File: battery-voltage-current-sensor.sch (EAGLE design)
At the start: 59 parts, among them IC1 ACS758LCB-050B-PFF-T, IC3 ADS1115IDGST

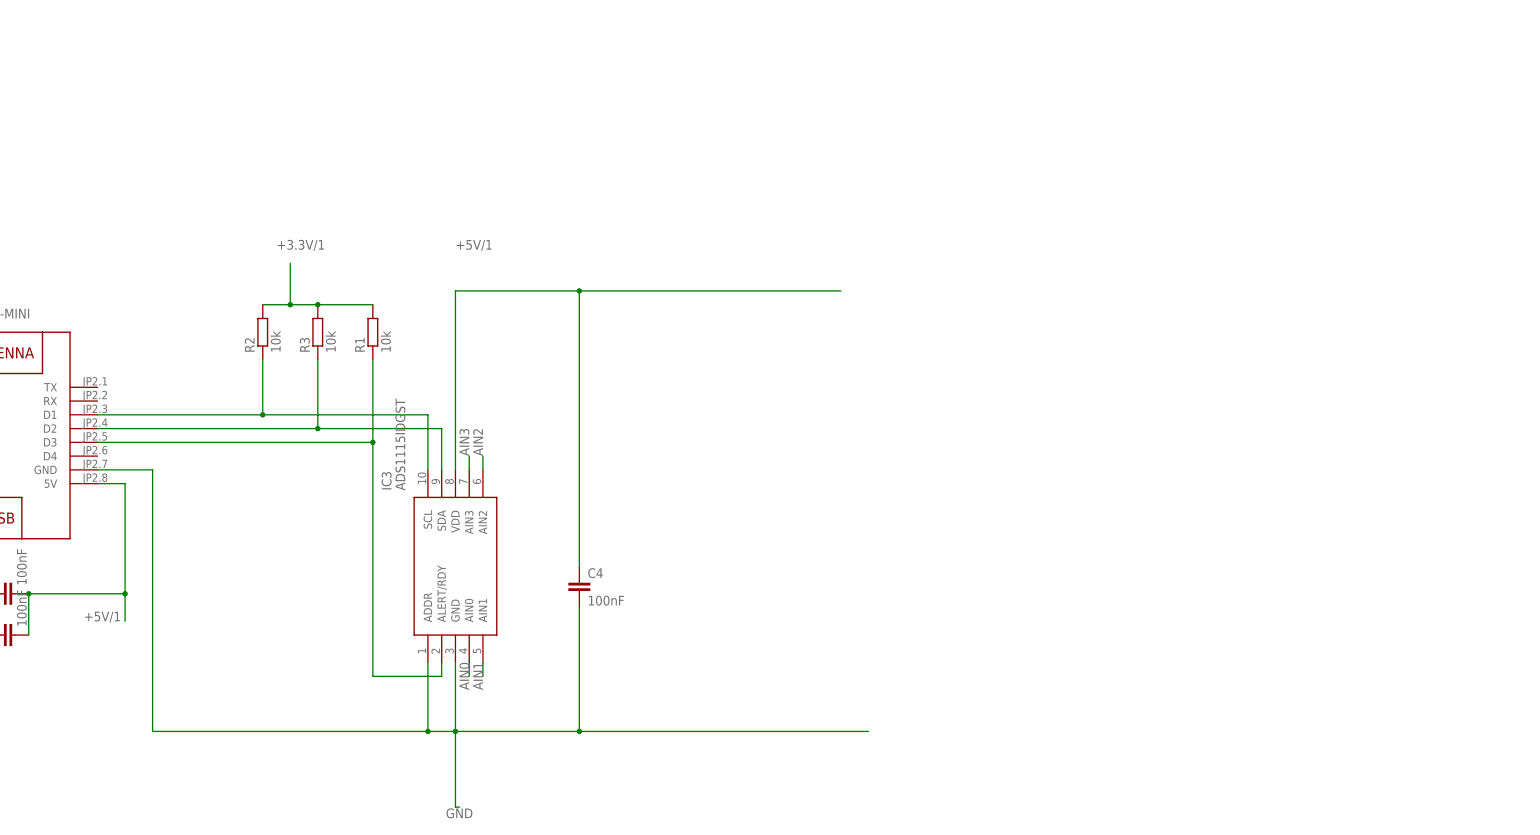
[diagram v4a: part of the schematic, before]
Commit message: level shifter added
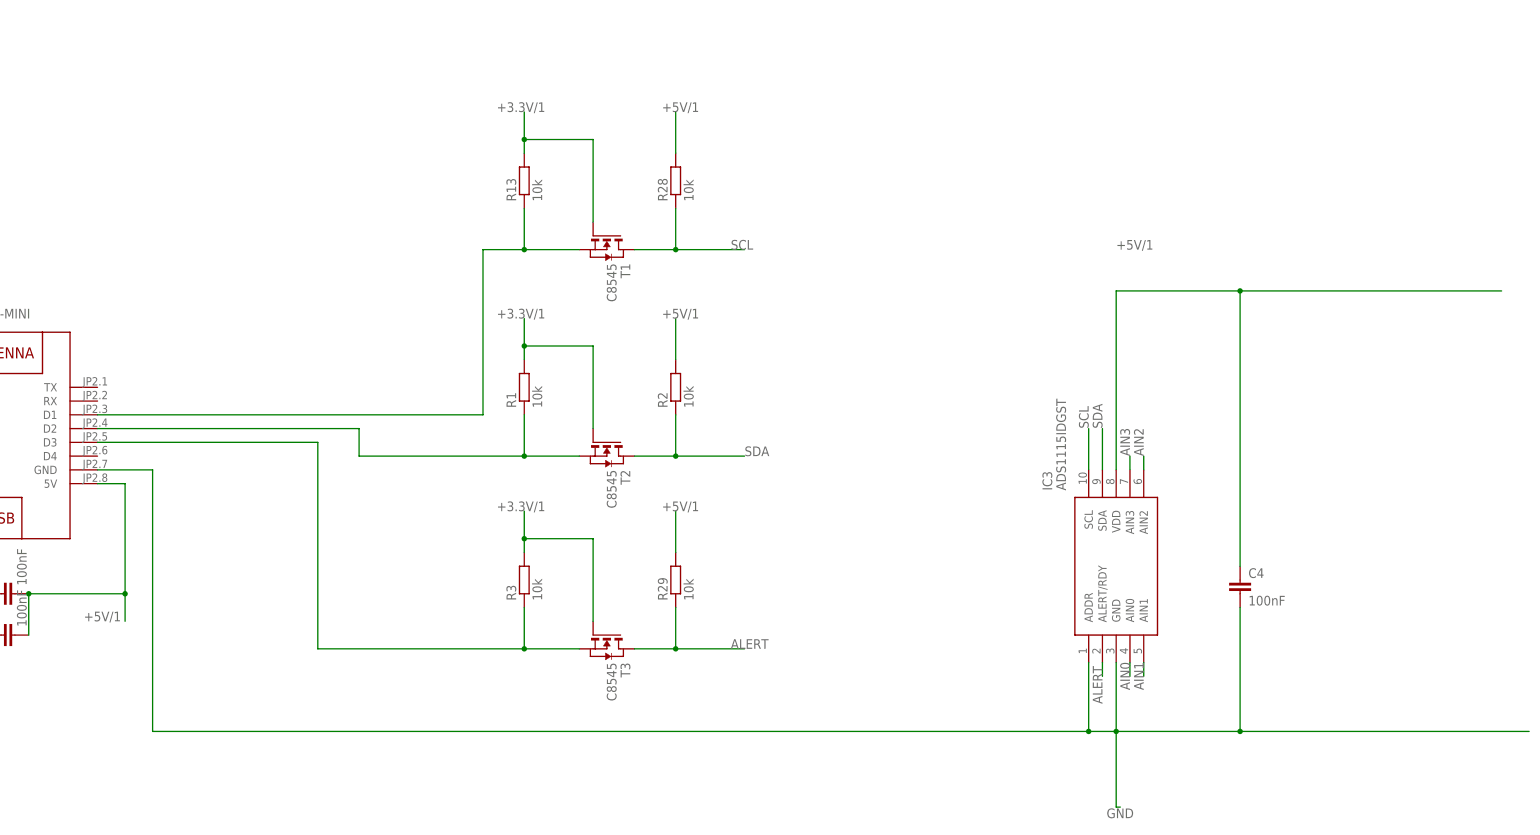
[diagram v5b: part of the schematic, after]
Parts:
- added R13, R28, R29: 10k, rcl:R-EU_R0603
- added T1, T2, T3: C8545, zetex:NMOSSOT23
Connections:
- removed net N$4: IC3.SCL, R2.1, U$1.D1
- new net ALERT: IC3.ALERT/RDY, R29.1, T3.D
- new net N$2: R13.1, T1.S, U$1.D1
- new net SCL: IC3.SCL, R28.1, T1.D
- new net SDA: IC3.SDA, R2.1, T2.D
- net +3.3V/1: now also R13.2, T1.G, T2.G, T3.G; no longer R2.2
- net +5V/1: now also R2.2, R28.2, R29.2
- net N$1: now also T2.S, U$1.D2; no longer IC3.ALERT/RDY, U$1.D3
- net N$5: now also T3.S, U$1.D3; no longer IC3.SDA, U$1.D2
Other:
- moved on the sheet: C4, IC3, R1, R2, R3

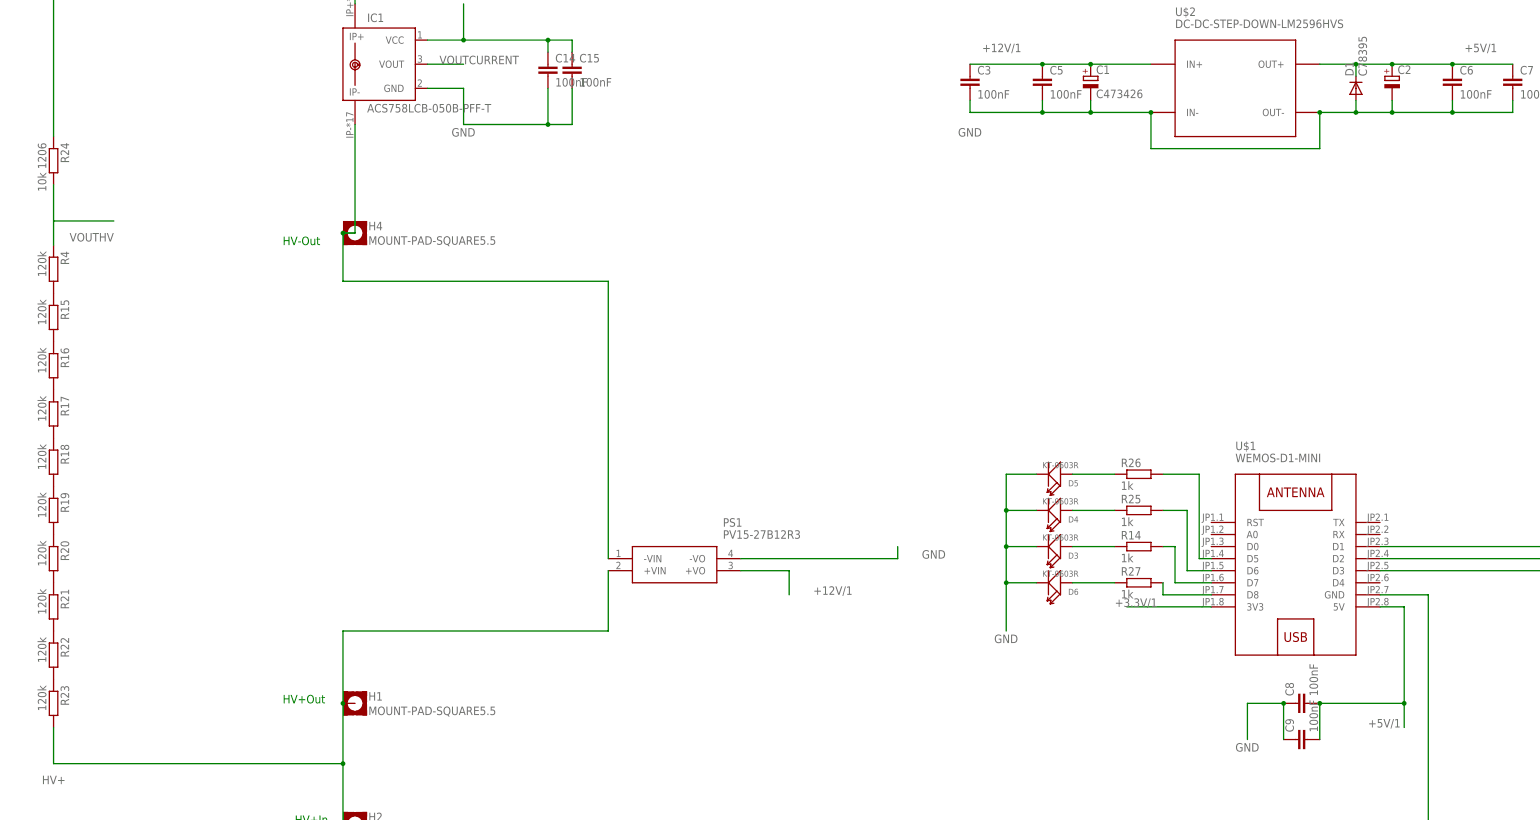
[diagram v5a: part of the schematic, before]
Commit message: external 12V added
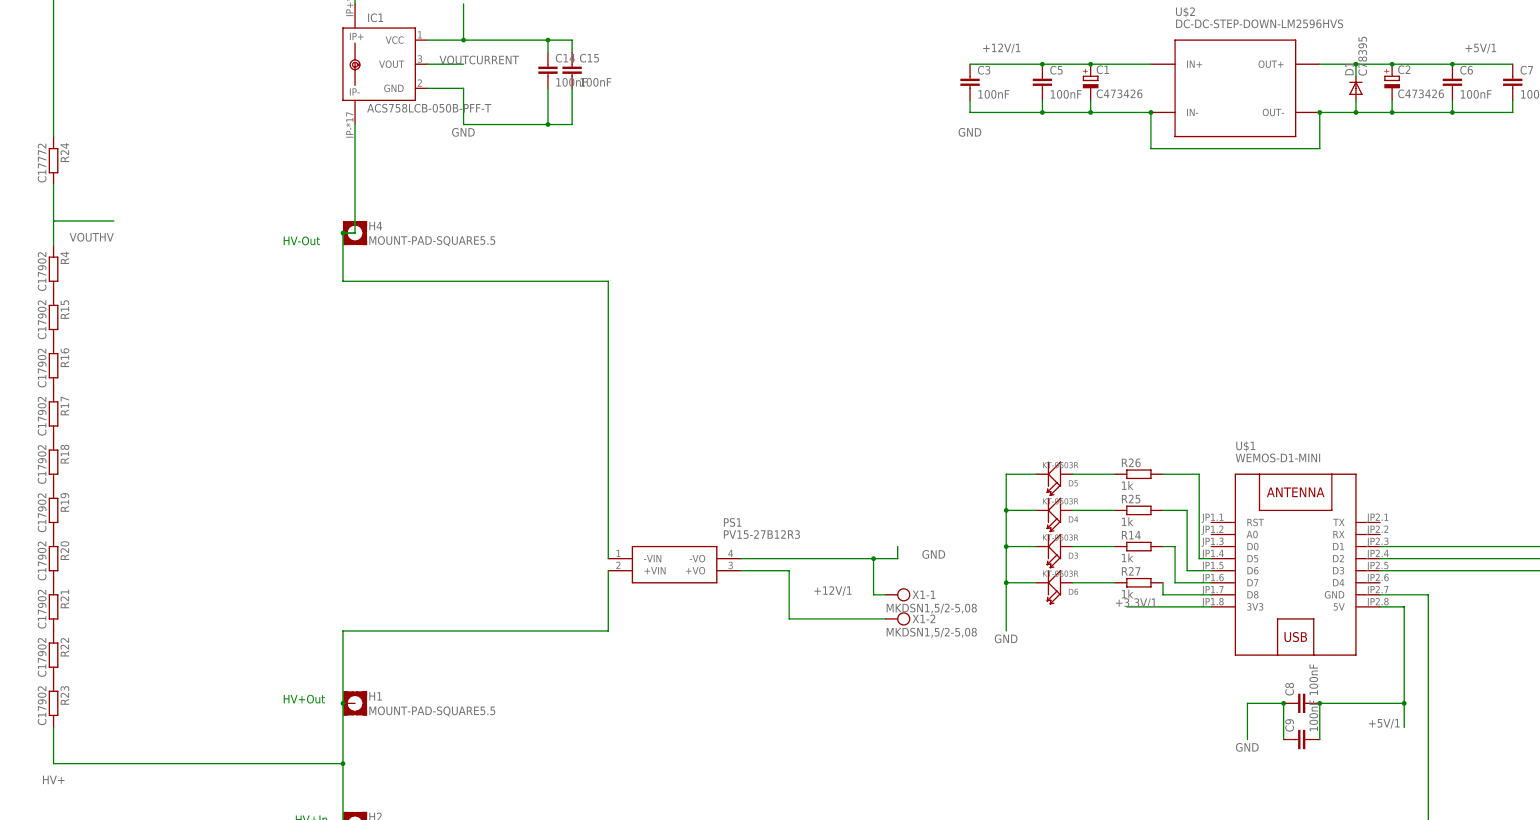
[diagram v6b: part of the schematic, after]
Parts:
- added X1: MKDSN1,5/2-5,08, con-phoenix-508:MKDSN1,5/2-5,08
- C2: value (none) -> C473426
- R15, R16, R17, R18, R19, R20, R21, R22, R23, R4: value 120k -> C17902
- R24: value 10k 1206 -> C17772; device rcl:R-EU_R1206 -> rcl:R-EU_R0805
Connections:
- net +12V/1: now also X1-2.KL
- net GND: now also X1-1.KL
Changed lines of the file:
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@@
 <part name="IC1" library="allegro" library_urn="urn:adsk.eagle:library:93" deviceset="ACS758*" device="" package3d_urn="urn:adsk.eagle:package:3449/1" technology="LCB-050B-PFF-T"/>
 <part name="IC3" library="SamacSys_Parts" deviceset="ADS1115IDGST" device=""/>
-<part name="R4" library="rcl" library_urn="urn:adsk.eagle:library:334" deviceset="R-EU_" device="R1206" package3d_urn="urn:adsk.eagle:package:23540/2" value="120k"/>
-<part name="R15" library="rcl" library_urn="urn:adsk.eagle:library:334" deviceset="R-EU_" device="R1206" package3d_urn="urn:adsk.eagle:package:23540/2" value="120k"/>
-<part name="R16" library="rcl" library_urn="urn:adsk.eagle:library:334" deviceset="R-EU_" device="R1206" package3d_urn="urn:adsk.eagle:package:23540/2" value="120k"/>
-<part name="R17" library="rcl" library_urn="urn:adsk.eagle:library:334" deviceset="R-EU_" device="R1206" package3d_urn="urn:adsk.eagle:package:23540/2" value="120k"/>
-<part name="R18" library="rcl" library_urn="urn:adsk.eagle:library:334" deviceset="R-EU_" device="R1206" package3d_urn="urn:adsk.eagle:package:23540/2" value="120k"/>
-<part name="R19" library="rcl" library_urn="urn:adsk.eagle:library:334" deviceset="R-EU_" device="R1206" package3d_urn="urn:adsk.eagle:package:23540/2" value="120k"/>
-<part name="R20" library="rcl" library_urn="urn:adsk.eagle:library:334" deviceset="R-EU_" device="R1206" package3d_urn="urn:adsk.eagle:package:23540/2" value="120k"/>
-<part name="R21" library="rcl" library_urn="urn:adsk.eagle:library:334" deviceset="R-EU_" device="R1206" package3d_urn="urn:adsk.eagle:package:23540/2" value="120k"/>
-<part name="R22" library="rcl" library_urn="urn:adsk.eagle:library:334" deviceset="R-EU_" device="R1206" package3d_urn="urn:adsk.eagle:package:23540/2" value="120k"/>
-<part name="R23" library="rcl" library_urn="urn:adsk.eagle:library:334" deviceset="R-EU_" device="R1206" package3d_urn="urn:adsk.eagle:package:23540/2" value="120k"/>
-<part name="R24" library="rcl" library_urn="urn:adsk.eagle:library:334" deviceset="R-EU_" device="R1206" package3d_urn="urn:adsk.eagle:package:23540/2" value="10k 1206"/>
+<part name="R4" library="rcl" library_urn="urn:adsk.eagle:library:334" deviceset="R-EU_" device="R1206" package3d_urn="urn:adsk.eagle:package:23540/2" value="C17902"/>
+<part name="R15" library="rcl" library_urn="urn:adsk.eagle:library:334" deviceset="R-EU_" device="R1206" package3d_urn="urn:adsk.eagle:package:23540/2" value="C17902"/>
+<part name="R16" library="rcl" library_urn="urn:adsk.eagle:library:334" deviceset="R-EU_" device="R1206" package3d_urn="urn:adsk.eagle:package:23540/2" value="C17902"/>
+<part name="R17" library="rcl" library_urn="urn:adsk.eagle:library:334" deviceset="R-EU_" device="R1206" package3d_urn="urn:adsk.eagle:package:23540/2" value="C17902"/>
+<part name="R18" library="rcl" library_urn="urn:adsk.eagle:library:334" deviceset="R-EU_" device="R1206" package3d_urn="urn:adsk.eagle:package:23540/2" value="C17902"/>
+<part name="R19" library="rcl" library_urn="urn:adsk.eagle:library:334" deviceset="R-EU_" device="R1206" package3d_urn="urn:adsk.eagle:package:23540/2" value="C17902"/>
+<part name="R20" library="rcl" library_urn="urn:adsk.eagle:library:334" deviceset="R-EU_" device="R1206" package3d_urn="urn:adsk.eagle:package:23540/2" value="C17902"/>
+<part name="R21" library="rcl" library_urn="urn:adsk.eagle:library:334" deviceset="R-EU_" device="R1206" package3d_urn="urn:adsk.eagle:package:23540/2" value="C17902"/>
+<part name="R22" library="rcl" library_urn="urn:adsk.eagle:library:334" deviceset="R-EU_" device="R1206" package3d_urn="urn:adsk.eagle:package:23540/2" value="C17902"/>
+<part name="R23" library="rcl" library_urn="urn:adsk.eagle:library:334" deviceset="R-EU_" device="R1206" package3d_urn="urn:adsk.eagle:package:23540/2" value="C17902"/>
+<part name="R24" library="rcl" library_urn="urn:adsk.eagle:library:334" deviceset="R-EU_" device="R0805" package3d_urn="urn:adsk.eagle:package:23553/2" value="C17772"/>
 <part name="C4" library="rcl" library_urn="urn:adsk.eagle:library:334" deviceset="C-EU" device="C0805" package3d_urn="urn:adsk.eagle:package:23617/2" value="100nF"/>
 <part name="U$2" library="diy-modules" deviceset="DC-DC-STEP-DOWN-LM2596HVS" device=""/>
 <part name="C1" library="rcl" library_urn="urn:adsk.eagle:library:334" deviceset="CPOL-EU" device="UD-6,3X7,7" package3d_urn="urn:adsk.eagle:package:23472/1" value="C473426"/>
-<part name="C2" library="rcl" library_urn="urn:adsk.eagle:library:334" deviceset="CPOL-EU" device="UD-6,3X7,7" package3d_urn="urn:adsk.eagle:package:23472/1"/>
+<part name="C2" library="rcl" library_urn="urn:adsk.eagle:library:334" deviceset="CPOL-EU" device="UD-6,3X7,7" package3d_urn="urn:adsk.eagle:package:23472/1" value="C473426"/>
 <part name="C3" library="rcl" library_urn="urn:adsk.eagle:library:334" deviceset="C-EU" device="C0603" package3d_urn="urn:adsk.eagle:package:23616/2" value="100nF"/>
 <part name="C5" library="rcl" library_urn="urn:adsk.eagle:library:334" deviceset="C-EU" device="C0603" package3d_urn="urn:adsk.eagle:package:23616/2" value="100nF"/>
@@
 <part name="R3" library="rcl" library_urn="urn:adsk.eagle:library:334" deviceset="R-EU_" device="R0603" package3d_urn="urn:adsk.eagle:package:23555/2" value="10k"/>
 <part name="R29" library="rcl" library_urn="urn:adsk.eagle:library:334" deviceset="R-EU_" device="R0603" package3d_urn="urn:adsk.eagle:package:23555/2" value="10k"/>
+<part name="X1" library="con-phoenix-508" library_urn="urn:adsk.eagle:library:176" deviceset="MKDSN1,5/2-5,08" device="" package3d_urn="urn:adsk.eagle:package:9630/1"/>
 </parts>
 <sheets>
@@
 <attribute name="NAME" x="321.0814" y="31.75" size="1.778" layer="95" rot="R90"/>
 <attribute name="VALUE" x="325.882" y="31.75" size="1.778" layer="96" rot="R90"/>
+</instance>
+<instance part="X1" gate="-1" x="114.3" y="55.88" smashed="yes">
+<attribute name="NAME" x="117.348" y="54.991" size="1.778" layer="95"/>
+<attribute name="VALUE" x="111.76" y="52.197" size="1.778" layer="96"/>
+</instance>
+<instance part="X1" gate="-2" x="114.3" y="50.8" smashed="yes">
+<attribute name="NAME" x="117.348" y="49.911" size="1.778" layer="95"/>
+<attribute name="VALUE" x="111.76" y="47.117" size="1.778" layer="96"/>
 </instance>
 </instances>
@@
 <segment>
 <pinref part="PS1" gate="G$1" pin="-VO"/>
-<wire x1="81.28" y1="63.5" x2="114.3" y2="63.5" width="0.1524" layer="91"/>
+<wire x1="81.28" y1="63.5" x2="109.22" y2="63.5" width="0.1524" layer="91"/>
+<wire x1="109.22" y1="63.5" x2="114.3" y2="63.5" width="0.1524" layer="91"/>
 <wire x1="114.3" y1="63.5" x2="114.3" y2="66.04" width="0.1524" layer="91"/>
 <label x="119.38" y="63.5" size="1.778" layer="95"/>
+<pinref part="X1" gate="-1" pin="KL"/>
+<wire x1="111.76" y1="55.88" x2="109.22" y2="55.88" width="0.1524" layer="91"/>
+<wire x1="109.22" y1="55.88" x2="109.22" y2="63.5" width="0.1524" layer="91"/>
+<junction x="109.22" y="63.5"/>
 </segment>
 <segment>
@@
 <pinref part="PS1" gate="G$1" pin="+VO"/>
 <wire x1="81.28" y1="60.96" x2="91.44" y2="60.96" width="0.1524" layer="91"/>
-<wire x1="91.44" y1="60.96" x2="91.44" y2="55.88" width="0.1524" layer="91"/>
 <label x="96.52" y="55.88" size="1.778" layer="95"/>
-</segment>
-<segment>
+<pinref part="X1" gate="-2" pin="KL"/>
+<wire x1="111.76" y1="50.8" x2="91.44" y2="50.8" width="0.1524" layer="91"/>
+<wire x1="91.44" y1="50.8" x2="91.44" y2="60.96" width="0.1524" layer="91"/>
+</segment>
+<segment>
